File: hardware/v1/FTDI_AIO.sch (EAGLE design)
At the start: 45 parts, among them IC1 MCP1702-3.3, IC2 FT232RL, X1 ISP, X2 USB-A-H, X3 UART

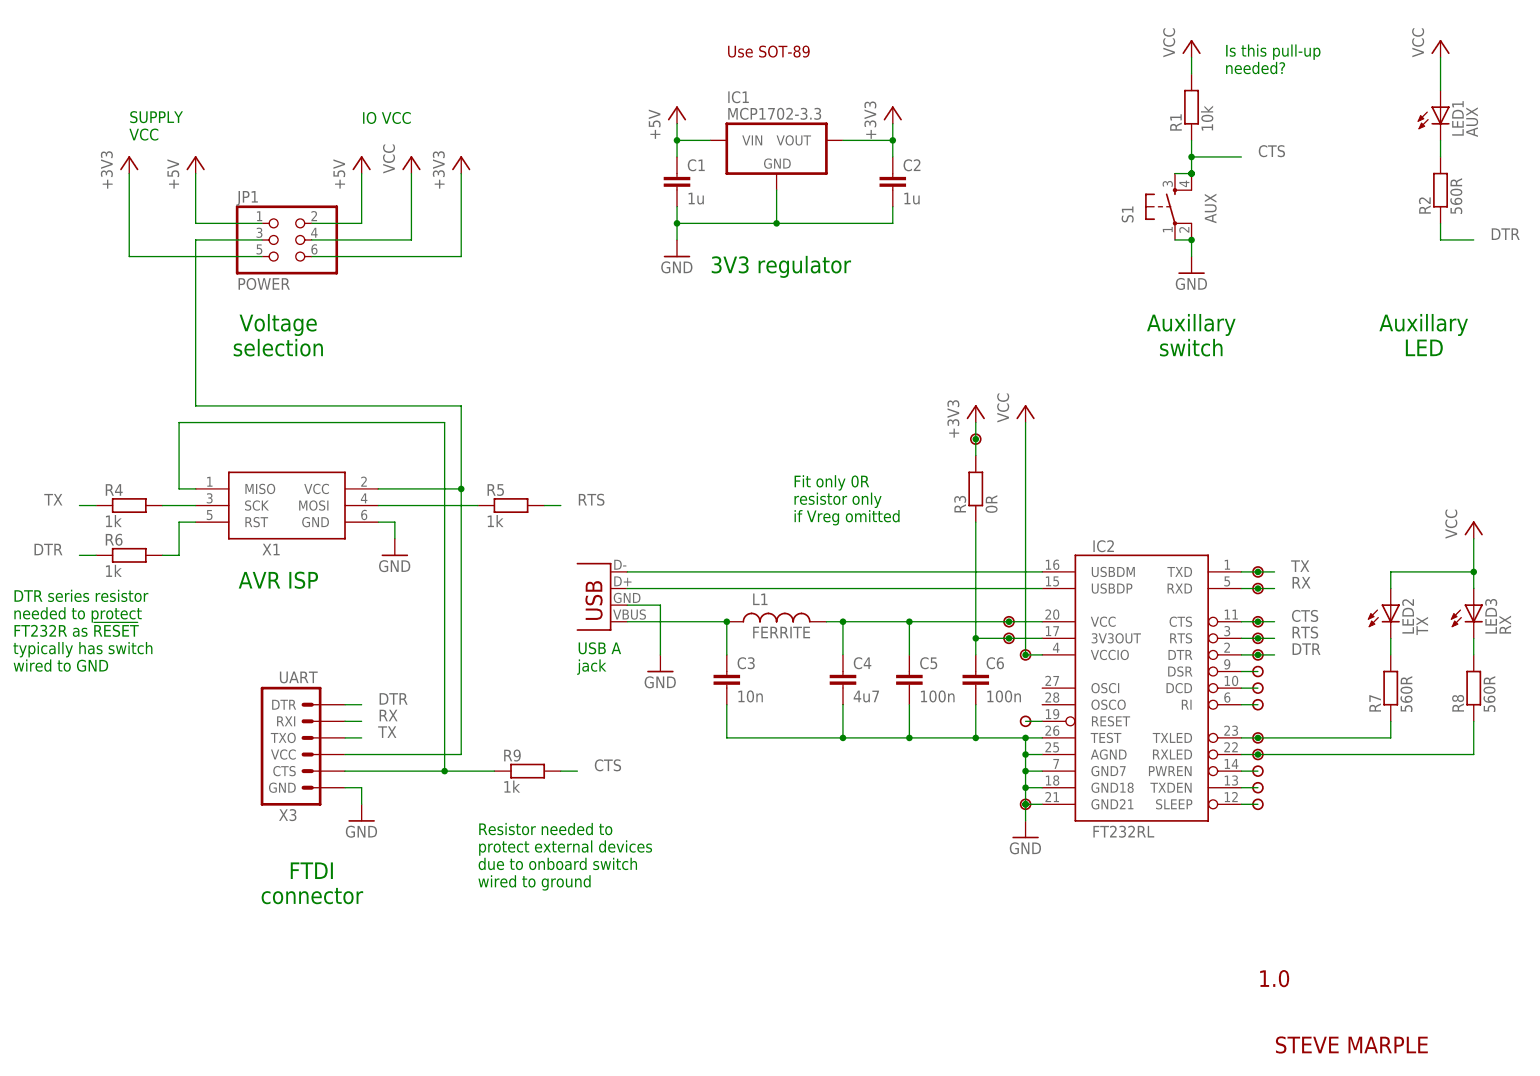
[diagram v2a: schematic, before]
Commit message: Updating to use modified FT232R package. Rerouted TXLED.
TXLED signal rerouted to avoid breaking ground place in vicinity of
USB data lines.
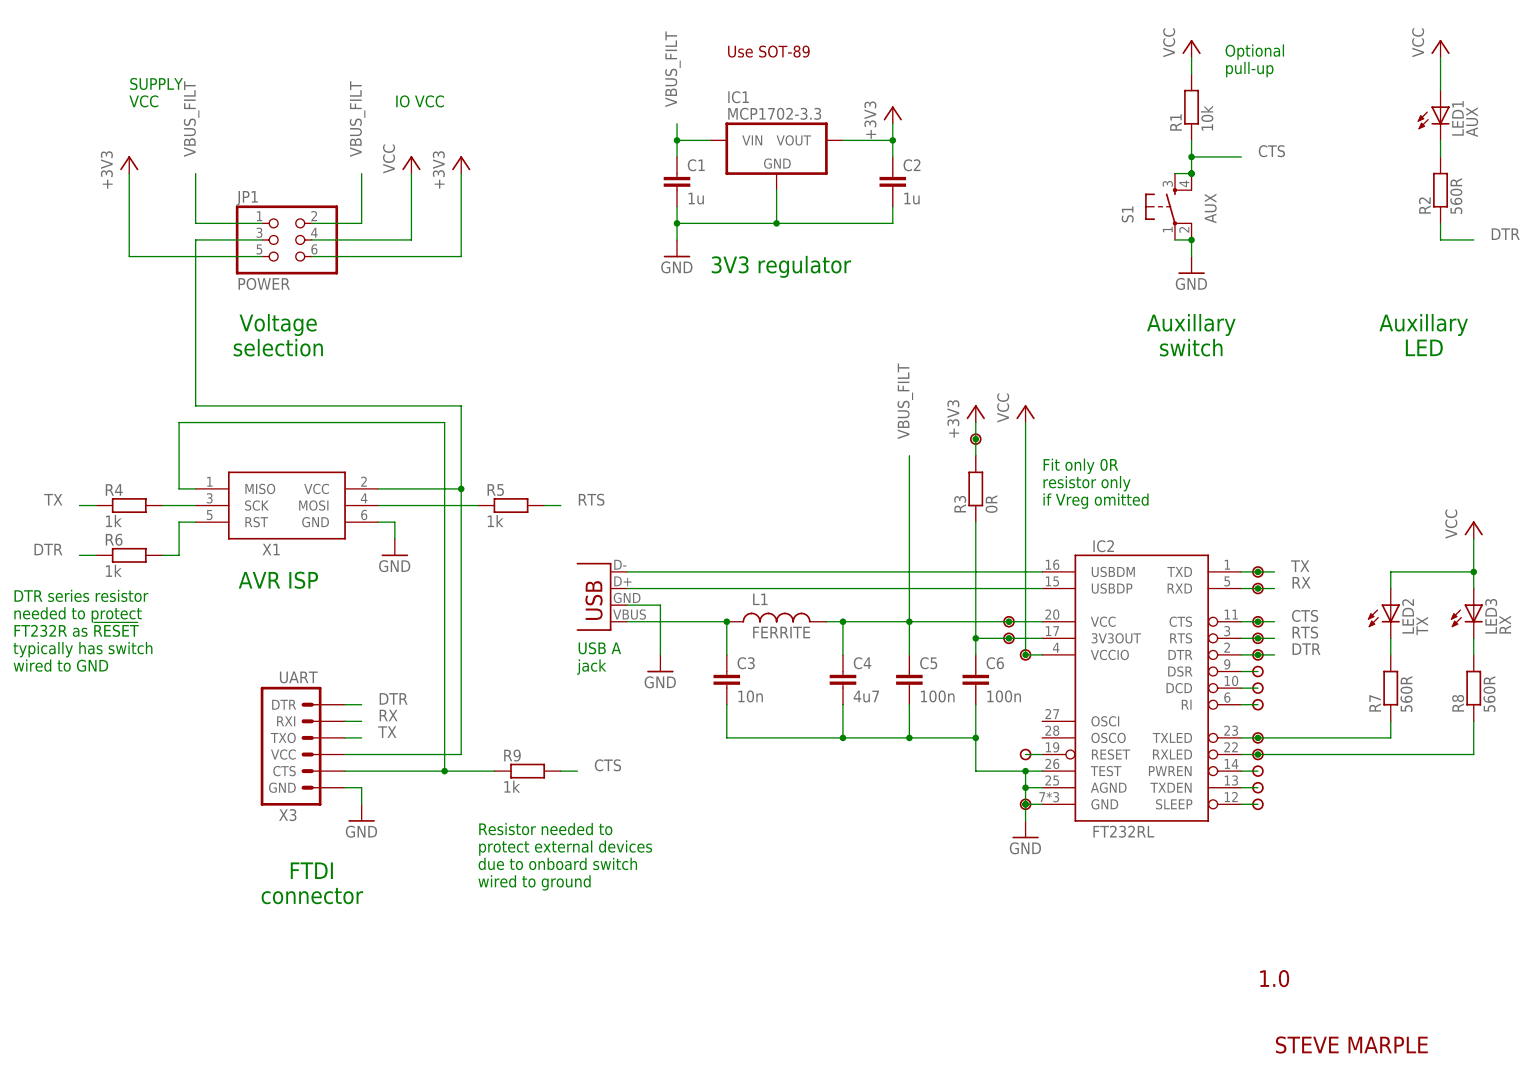
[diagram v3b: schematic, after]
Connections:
- net N$11 renamed TXLED
- net N$12 renamed RXLED
- net N$26 renamed !RESET
- removed net +5V: C1.1, IC1.VIN, JP1.1, JP1.2
- removed net VUSB_FILT: C4.1, C5.1, IC2.VCC, L1.2, U$4.1
- new net VBUS_FILT: C1.1, C4.1, C5.1, IC1.VIN, IC2.VCC, JP1.1, JP1.2, L1.2, U$4.1
- net GND: now also IC2.GND; no longer IC2.GND18, IC2.GND21, IC2.GND7
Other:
- note added: "Optional pull-up"
- note removed: "Is this pull-up needed?"
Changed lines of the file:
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@@
 <?xml version="1.0" encoding="utf-8"?>
 <!DOCTYPE eagle SYSTEM "eagle.dtd">
-<eagle version="6.5.0">
+<eagle version="6.4">
 <drawing>
 <settings>
@@
 <class number="1" name="power" width="0" drill="0">
 </class>
-<class number="2" name="Vusb_filt" width="0.3048" drill="0">
+<class number="2" name="Vbus" width="0.3048" drill="0">
 </class>
 </classes>
@@
 <part name="JP1" library="pinhead" deviceset="PINHD-2X3" device="" value="POWER"/>
 <part name="P+1" library="supply1" deviceset="VCC" device=""/>
-<part name="P+5" library="supply1" deviceset="+5V" device=""/>
 <part name="+3V5" library="supply1" deviceset="+3V3" device=""/>
-<part name="P+6" library="supply1" deviceset="+5V" device=""/>
 <part name="+3V1" library="supply1" deviceset="+3V3" device=""/>
 <part name="X1" library="SteveMarple" deviceset="AVRISP" device="-HEADER-6-SHROUDED" value="ISP"/>
@@
 <part name="C2" library="SteveMarple" deviceset="C-EU" device="1206-HAND" value="1u"/>
 <part name="GND34" library="supply1" deviceset="GND" device=""/>
-<part name="P+8" library="supply1" deviceset="+5V" device=""/>
 <part name="R3" library="SteveMarple" deviceset="RESISTOR" device="1206-HAND" value="0R"/>
 <part name="+3V2" library="supply1" deviceset="+3V3" device=""/>
@@
 <text x="58.42" y="27.94" size="2.54" layer="91" align="bottom-center">FTDI
 connector</text>
-<text x="198.12" y="154.94" size="1.778" layer="91">Is this pull-up
-needed?</text>
-<text x="66.04" y="147.32" size="1.778" layer="91">IO VCC</text>
-<text x="30.48" y="144.78" size="1.778" layer="91">SUPPLY
+<text x="198.12" y="154.94" size="1.778" layer="91">Optional
+pull-up</text>
+<text x="71.12" y="149.86" size="1.778" layer="91">IO VCC</text>
+<text x="30.48" y="149.86" size="1.778" layer="91">SUPPLY
 VCC</text>
 <text x="53.34" y="76.2" size="2.54" layer="91" align="bottom-center">AVR ISP</text>
@@
 <text x="119.38" y="124.46" size="2.54" layer="91">3V3 regulator</text>
 <text x="121.92" y="157.48" size="1.778" layer="94">Use SOT-89</text>
-<text x="132.08" y="86.36" size="1.778" layer="91">Fit only 0R
+<text x="170.18" y="88.9" size="1.778" layer="91">Fit only 0R
 resistor only
 if Vreg omitted</text>
@@
 <instance part="JP1" gate="A" x="53.34" y="129.54"/>
 <instance part="P+1" gate="VCC" x="73.66" y="142.24"/>
-<instance part="P+5" gate="1" x="66.04" y="142.24"/>
 <instance part="+3V5" gate="G$1" x="81.28" y="142.24"/>
-<instance part="P+6" gate="1" x="40.64" y="142.24"/>
 <instance part="+3V1" gate="G$1" x="30.48" y="142.24"/>
 <instance part="X1" gate="G$1" x="53.34" y="88.9"/>
@@
 <instance part="C2" gate="G$1" x="147.32" y="139.7"/>
 <instance part="GND34" gate="1" x="114.3" y="127"/>
-<instance part="P+8" gate="1" x="114.3" y="149.86"/>
 <instance part="R3" gate="G$1" x="160.02" y="91.44" rot="R90"/>
 <instance part="+3V2" gate="G$1" x="160.02" y="104.14"/>
@@
 <instance part="U$19" gate="G$1" x="203.2" y="43.18"/>
 <instance part="U$18" gate="G$1" x="167.64" y="43.18"/>
-<instance part="U$13" gate="G$1" x="167.64" y="55.88"/>
+<instance part="U$13" gate="G$1" x="167.64" y="50.8"/>
 <instance part="C5" gate="G$1" x="149.86" y="63.5"/>
 <instance part="C4" gate="G$1" x="139.7" y="63.5"/>
@@
 </segment>
 <segment>
-<pinref part="IC2" gate="G$1" pin="AGND"/>
-<wire x1="170.18" y1="50.8" x2="167.64" y2="50.8" width="0.1524" layer="91"/>
 <pinref part="GND28" gate="1" pin="GND"/>
-<wire x1="167.64" y1="50.8" x2="167.64" y2="48.26" width="0.1524" layer="91"/>
 <junction x="167.64" y="43.18"/>
 <wire x1="167.64" y1="48.26" x2="167.64" y2="45.72" width="0.1524" layer="91"/>
@@
 <junction x="167.64" y="45.72"/>
 <junction x="167.64" y="48.26"/>
-<pinref part="IC2" gate="G$1" pin="GND7"/>
+<pinref part="IC2" gate="G$1" pin="TEST"/>
 <wire x1="170.18" y1="48.26" x2="167.64" y2="48.26" width="0.1524" layer="91"/>
-<pinref part="IC2" gate="G$1" pin="GND18"/>
+<pinref part="IC2" gate="G$1" pin="AGND"/>
 <wire x1="170.18" y1="45.72" x2="167.64" y2="45.72" width="0.1524" layer="91"/>
-<pinref part="IC2" gate="G$1" pin="GND21"/>
+<pinref part="IC2" gate="G$1" pin="GND"/>
 <wire x1="170.18" y1="43.18" x2="167.64" y2="43.18" width="0.1524" layer="91"/>
-<junction x="167.64" y="50.8"/>
 <pinref part="C6" gate="G$1" pin="2"/>
-<wire x1="167.64" y1="50.8" x2="167.64" y2="53.34" width="0.1524" layer="91"/>
-<wire x1="167.64" y1="53.34" x2="160.02" y2="53.34" width="0.1524" layer="91"/>
 <wire x1="160.02" y1="53.34" x2="160.02" y2="58.42" width="0.1524" layer="91"/>
 <pinref part="U$18" gate="G$1" pin="1"/>
 <junction x="167.64" y="43.18"/>
-<junction x="167.64" y="53.34"/>
-<pinref part="IC2" gate="G$1" pin="TEST"/>
-<wire x1="170.18" y1="53.34" x2="167.64" y2="53.34" width="0.1524" layer="91"/>
 <junction x="160.02" y="53.34"/>
 <pinref part="C4" gate="G$1" pin="2"/>
@@
 <wire x1="121.92" y1="58.42" x2="121.92" y2="53.34" width="0.1524" layer="91"/>
 <wire x1="121.92" y1="53.34" x2="139.7" y2="53.34" width="0.1524" layer="91"/>
+<wire x1="160.02" y1="53.34" x2="160.02" y2="48.26" width="0.1524" layer="91"/>
+<wire x1="160.02" y1="48.26" x2="167.64" y2="48.26" width="0.1524" layer="91"/>
 </segment>
 <segment>
@@
 </segment>
 </net>
-<net name="VUSB_FILT" class="2">
+<net name="VBUS_FILT" class="2">
 <segment>
 <pinref part="IC2" gate="G$1" pin="VCC"/>
@@
 <junction x="165.1" y="71.12"/>
 <pinref part="L1" gate="G$1" pin="2"/>
+<wire x1="149.86" y1="71.12" x2="149.86" y2="96.52" width="0.1524" layer="91"/>
+<label x="149.86" y="99.06" size="1.778" layer="95" rot="R90"/>
+</segment>
+<segment>
+<wire x1="40.64" y1="139.7" x2="40.64" y2="132.08" width="0.1524" layer="91"/>
+<pinref part="JP1" gate="A" pin="1"/>
+<wire x1="40.64" y1="132.08" x2="50.8" y2="132.08" width="0.1524" layer="91"/>
+<label x="40.64" y="142.24" size="1.778" layer="95" rot="R90"/>
+</segment>
+<segment>
+<pinref part="JP1" gate="A" pin="2"/>
+<wire x1="58.42" y1="132.08" x2="66.04" y2="132.08" width="0.1524" layer="91"/>
+<wire x1="66.04" y1="132.08" x2="66.04" y2="139.7" width="0.1524" layer="91"/>
+<label x="66.04" y="142.24" size="1.778" layer="95" rot="R90"/>
+</segment>
+<segment>
+<wire x1="119.38" y1="144.78" x2="114.3" y2="144.78" width="0.1524" layer="91"/>
+<wire x1="114.3" y1="142.24" x2="114.3" y2="144.78" width="0.1524" layer="91"/>
+<pinref part="IC1" gate="G$1" pin="VIN"/>
+<pinref part="C1" gate="G$1" pin="1"/>
+<junction x="114.3" y="144.78"/>
+<wire x1="114.3" y1="144.78" x2="114.3" y2="147.32" width="0.1524" layer="91"/>
+<label x="114.3" y="149.86" size="1.778" layer="95" rot="R90"/>
 </segment>
 </net>
@@
 </segment>
 </net>
-<net name="N$11" class="0">
+<net name="TXLED" class="0">
 <segment>
 <pinref part="R7" gate="G$1" pin="1"/>
@@
 </segment>
 </net>
-<net name="N$12" class="0">
+<net name="RXLED" class="0">
 <segment>
 <pinref part="IC2" gate="G$1" pin="RXLED"/>
@@
 </segment>
 </net>
-<net name="+5V" class="0">
-<segment>
-<pinref part="JP1" gate="A" pin="2"/>
-<wire x1="58.42" y1="132.08" x2="66.04" y2="132.08" width="0.1524" layer="91"/>
-<pinref part="P+5" gate="1" pin="+5V"/>
-<wire x1="66.04" y1="132.08" x2="66.04" y2="139.7" width="0.1524" layer="91"/>
-</segment>
-<segment>
-<pinref part="P+6" gate="1" pin="+5V"/>
-<wire x1="40.64" y1="139.7" x2="40.64" y2="132.08" width="0.1524" layer="91"/>
-<pinref part="JP1" gate="A" pin="1"/>
-<wire x1="40.64" y1="132.08" x2="50.8" y2="132.08" width="0.1524" layer="91"/>
-</segment>
-<segment>
-<wire x1="119.38" y1="144.78" x2="114.3" y2="144.78" width="0.1524" layer="91"/>
-<wire x1="114.3" y1="142.24" x2="114.3" y2="144.78" width="0.1524" layer="91"/>
-<pinref part="IC1" gate="G$1" pin="VIN"/>
-<pinref part="C1" gate="G$1" pin="1"/>
-<pinref part="P+8" gate="1" pin="+5V"/>
-<junction x="114.3" y="144.78"/>
-<wire x1="114.3" y1="144.78" x2="114.3" y2="147.32" width="0.1524" layer="91"/>
-</segment>
-</net>
 <net name="+3V3" class="0">
 <segment>
@@
 </segment>
 </net>
-<net name="N$26" class="0">
-<segment>
-<pinref part="IC2" gate="G$1" pin="RESET"/>
-<pinref part="U$13" gate="G$1" pin="1"/>
-<wire x1="170.18" y1="55.88" x2="167.64" y2="55.88" width="0.1524" layer="91"/>
-</segment>
-</net>
 <net name="RTS" class="0">
 <segment>
@@
 </segment>
 </net>
+<net name="!RESET" class="0">
+<segment>
+<pinref part="IC2" gate="G$1" pin="RESET"/>
+<pinref part="U$13" gate="G$1" pin="1"/>
+<wire x1="167.64" y1="50.8" x2="170.18" y2="50.8" width="0.1524" layer="91"/>
+</segment>
+</net>

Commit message: Adding decoupling capacitor for FT232R VCCIO.
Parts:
- added C7: 100n, SteveMarple:C-EU1206-HAND
- C3: value 10n -> 100n
- C4: value 4u7 -> 10n
- C5: value 100n -> 4u7
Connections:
- net !RESET: now also U$14.1; no longer U$13.1
- net 3V3_OUT: now also C7.1; no longer C6.1
- net GND: now also C7.2
- net TXLED: now also U$13.1; no longer U$14.1
- net VBUS_FILT: now also C6.1; no longer C4.1
- net VCC: now also C3.1
- net VUSB: now also C4.1; no longer C3.1
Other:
- moved on the sheet: C3, C4, C5, C6, JP1

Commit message: Ensuring all silkscreen is within board outline.
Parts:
- X2: device SparkFun:USB-A-H -> SteveMarple:USB-A-H
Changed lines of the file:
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@@
 <part name="LED1" library="SparkFun" deviceset="LED" device="3MM" value="AUX"/>
 <part name="R2" library="SteveMarple" deviceset="RESISTOR" device="1206-HAND" value="560R"/>
-<part name="X2" library="SparkFun" deviceset="USB" device="-A-H"/>
+<part name="X2" library="SteveMarple" deviceset="USB" device="-A-H"/>
 <part name="IC1" library="SteveMarple" deviceset="MCP1702" device="" value="MCP1702-3.3"/>
 <part name="+3V6" library="supply1" deviceset="+3V3" device=""/>
